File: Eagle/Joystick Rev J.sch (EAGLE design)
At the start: 20 parts, among them U3 LM317-BENT

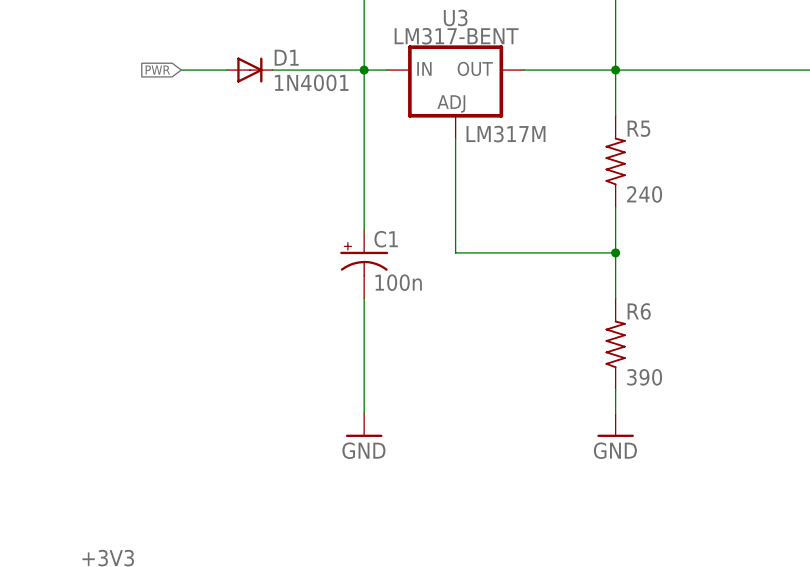
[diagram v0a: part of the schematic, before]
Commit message: changes to BOM for manufacturing
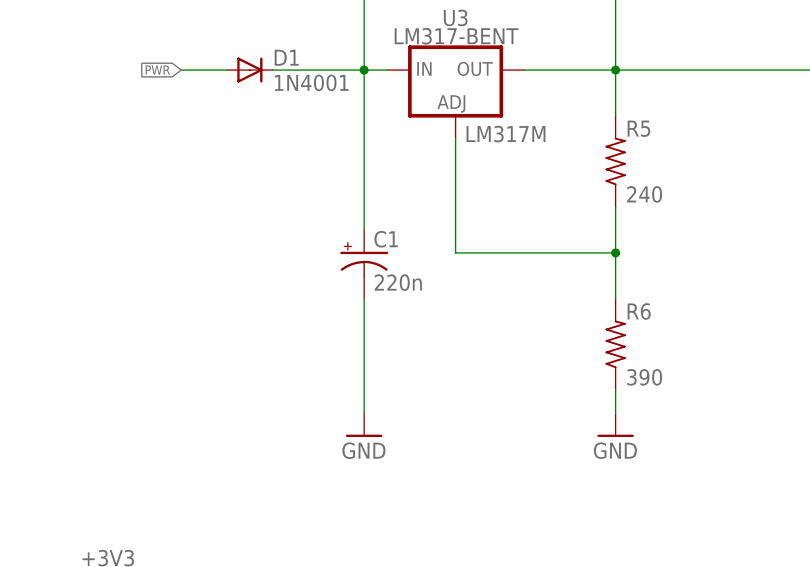
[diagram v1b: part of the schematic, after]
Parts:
- C1: value 100n -> 220n
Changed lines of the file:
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@@
 <grid distance="0.1" unitdist="inch" unit="inch" style="lines" multiple="1" display="no" altdistance="0.01" altunitdist="inch" altunit="inch"/>
 <layers>
-<layer number="1" name="Top" color="4" fill="1" visible="yes" active="no"/>
-<layer number="2" name="Route2" color="16" fill="1" visible="yes" active="no"/>
-<layer number="3" name="Route3" color="4" fill="3" visible="yes" active="no"/>
-<layer number="4" name="Route4" color="1" fill="4" visible="yes" active="no"/>
-<layer number="5" name="Route5" color="4" fill="4" visible="yes" active="no"/>
-<layer number="6" name="Route6" color="1" fill="8" visible="yes" active="no"/>
-<layer number="7" name="Route7" color="4" fill="8" visible="yes" active="no"/>
-<layer number="8" name="Route8" color="1" fill="2" visible="yes" active="no"/>
-<layer number="9" name="Route9" color="4" fill="2" visible="yes" active="no"/>
-<layer number="10" name="Route10" color="1" fill="7" visible="yes" active="no"/>
-<layer number="11" name="Route11" color="4" fill="7" visible="yes" active="no"/>
-<layer number="12" name="Route12" color="1" fill="5" visible="yes" active="no"/>
-<layer number="13" name="Route13" color="4" fill="5" visible="yes" active="no"/>
-<layer number="14" name="Route14" color="1" fill="6" visible="yes" active="no"/>
-<layer number="15" name="Route15" color="23" fill="1" visible="yes" active="no"/>
-<layer number="16" name="Bottom" color="1" fill="1" visible="yes" active="no"/>
-<layer number="17" name="Pads" color="2" fill="1" visible="yes" active="no"/>
-<layer number="18" name="Vias" color="2" fill="1" visible="yes" active="no"/>
-<layer number="19" name="Unrouted" color="6" fill="1" visible="yes" active="no"/>
-<layer number="20" name="Dimension" color="24" fill="1" visible="yes" active="no"/>
-<layer number="21" name="tPlace" color="7" fill="1" visible="yes" active="no"/>
-<layer number="22" name="bPlace" color="7" fill="1" visible="yes" active="no"/>
-<layer number="23" name="tOrigins" color="15" fill="1" visible="yes" active="no"/>
-<layer number="24" name="bOrigins" color="15" fill="1" visible="yes" active="no"/>
-<layer number="25" name="tNames" color="7" fill="1" visible="yes" active="no"/>
-<layer number="26" name="bNames" color="7" fill="1" visible="yes" active="no"/>
-<layer number="27" name="tValues" color="7" fill="1" visible="yes" active="no"/>
-<layer number="28" name="bValues" color="7" fill="1" visible="yes" active="no"/>
+<layer number="1" name="Top" color="4" fill="1" visible="no" active="no"/>
+<layer number="2" name="Route2" color="16" fill="1" visible="no" active="no"/>
+<layer number="3" name="Route3" color="4" fill="3" visible="no" active="no"/>
+<layer number="4" name="Route4" color="1" fill="4" visible="no" active="no"/>
+<layer number="5" name="Route5" color="4" fill="4" visible="no" active="no"/>
+<layer number="6" name="Route6" color="1" fill="8" visible="no" active="no"/>
+<layer number="7" name="Route7" color="4" fill="8" visible="no" active="no"/>
+<layer number="8" name="Route8" color="1" fill="2" visible="no" active="no"/>
+<layer number="9" name="Route9" color="4" fill="2" visible="no" active="no"/>
+<layer number="10" name="Route10" color="1" fill="7" visible="no" active="no"/>
+<layer number="11" name="Route11" color="4" fill="7" visible="no" active="no"/>
+<layer number="12" name="Route12" color="1" fill="5" visible="no" active="no"/>
+<layer number="13" name="Route13" color="4" fill="5" visible="no" active="no"/>
+<layer number="14" name="Route14" color="1" fill="6" visible="no" active="no"/>
+<layer number="15" name="Route15" color="23" fill="1" visible="no" active="no"/>
+<layer number="16" name="Bottom" color="1" fill="1" visible="no" active="no"/>
+<layer number="17" name="Pads" color="2" fill="1" visible="no" active="no"/>
+<layer number="18" name="Vias" color="2" fill="1" visible="no" active="no"/>
+<layer number="19" name="Unrouted" color="6" fill="1" visible="no" active="no"/>
+<layer number="20" name="Dimension" color="24" fill="1" visible="no" active="no"/>
+<layer number="21" name="tPlace" color="7" fill="1" visible="no" active="no"/>
+<layer number="22" name="bPlace" color="7" fill="1" visible="no" active="no"/>
+<layer number="23" name="tOrigins" color="15" fill="1" visible="no" active="no"/>
+<layer number="24" name="bOrigins" color="15" fill="1" visible="no" active="no"/>
+<layer number="25" name="tNames" color="7" fill="1" visible="no" active="no"/>
+<layer number="26" name="bNames" color="7" fill="1" visible="no" active="no"/>
+<layer number="27" name="tValues" color="7" fill="1" visible="no" active="no"/>
+<layer number="28" name="bValues" color="7" fill="1" visible="no" active="no"/>
 <layer number="29" name="tStop" color="7" fill="3" visible="no" active="no"/>
 <layer number="30" name="bStop" color="7" fill="6" visible="no" active="no"/>
@@
 <layer number="35" name="tGlue" color="7" fill="4" visible="no" active="no"/>
 <layer number="36" name="bGlue" color="7" fill="5" visible="no" active="no"/>
-<layer number="37" name="tTest" color="7" fill="1" visible="yes" active="no"/>
-<layer number="38" name="bTest" color="7" fill="1" visible="yes" active="no"/>
+<layer number="37" name="tTest" color="7" fill="1" visible="no" active="no"/>
+<layer number="38" name="bTest" color="7" fill="1" visible="no" active="no"/>
 <layer number="39" name="tKeepout" color="4" fill="11" visible="no" active="no"/>
 <layer number="40" name="bKeepout" color="1" fill="11" visible="no" active="no"/>
@@
 <layer number="44" name="Drills" color="7" fill="1" visible="no" active="no"/>
 <layer number="45" name="Holes" color="7" fill="1" visible="no" active="no"/>
-<layer number="46" name="Milling" color="3" fill="1" visible="yes" active="no"/>
-<layer number="47" name="Measures" color="7" fill="1" visible="yes" active="no"/>
-<layer number="48" name="Document" color="7" fill="1" visible="yes" active="no"/>
-<layer number="49" name="Reference" color="7" fill="1" visible="yes" active="no"/>
-<layer number="50" name="dxf" color="7" fill="1" visible="yes" active="no"/>
-<layer number="51" name="tDocu" color="7" fill="1" visible="yes" active="no"/>
-<layer number="52" name="bDocu" color="7" fill="1" visible="yes" active="no"/>
-<layer number="53" name="tGND_GNDA" color="7" fill="9" visible="yes" active="no"/>
-<layer number="54" name="bGND_GNDA" color="1" fill="9" visible="yes" active="no"/>
-<layer number="56" name="wert" color="7" fill="1" visible="yes" active="no"/>
-<layer number="57" name="tCAD" color="7" fill="1" visible="yes" active="no"/>
-<layer number="58" name="tCAD" color="7" fill="1" visible="yes" active="no"/>
-<layer number="59" name="tCarbon" color="7" fill="1" visible="yes" active="no"/>
-<layer number="60" name="bCarbon" color="7" fill="1" visible="yes" active="no"/>
+<layer number="46" name="Milling" color="3" fill="1" visible="no" active="no"/>
+<layer number="47" name="Measures" color="7" fill="1" visible="no" active="no"/>
+<layer number="48" name="Document" color="7" fill="1" visible="no" active="no"/>
+<layer number="49" name="Reference" color="7" fill="1" visible="no" active="no"/>
+<layer number="50" name="dxf" color="7" fill="1" visible="no" active="no"/>
+<layer number="51" name="tDocu" color="7" fill="1" visible="no" active="no"/>
+<layer number="52" name="bDocu" color="7" fill="1" visible="no" active="no"/>
+<layer number="53" name="tGND_GNDA" color="7" fill="9" visible="no" active="no"/>
+<layer number="54" name="bGND_GNDA" color="1" fill="9" visible="no" active="no"/>
+<layer number="56" name="wert" color="7" fill="1" visible="no" active="no"/>
+<layer number="57" name="tCAD" color="7" fill="1" visible="no" active="no"/>
+<layer number="58" name="tCAD" color="7" fill="1" visible="no" active="no"/>
+<layer number="59" name="tCarbon" color="7" fill="1" visible="no" active="no"/>
+<layer number="60" name="bCarbon" color="7" fill="1" visible="no" active="no"/>
 <layer number="88" name="SimResults" color="9" fill="1" visible="yes" active="yes"/>
 <layer number="89" name="SimProbes" color="9" fill="1" visible="yes" active="yes"/>
@@
 <part name="D1" library="Quantum Projects" library_urn="urn:adsk.eagle:library:19630877" deviceset="1N4000" device="" package3d_urn="urn:adsk.eagle:package:20494835/2" value="1N4001"/>
 <part name="D2" library="Quantum Projects" library_urn="urn:adsk.eagle:library:19630877" deviceset="1N4000" device="" package3d_urn="urn:adsk.eagle:package:20494835/2" value="1N4001"/>
-<part name="C1" library="Quantum Projects" library_urn="urn:adsk.eagle:library:19630877" deviceset="ELECTROLYTIC-CAPACITOR" device="2-4" package3d_urn="urn:adsk.eagle:package:21734552/2" value="100n"/>
+<part name="C1" library="Quantum Projects" library_urn="urn:adsk.eagle:library:19630877" deviceset="ELECTROLYTIC-CAPACITOR" device="2-4" package3d_urn="urn:adsk.eagle:package:21734552/2" value="220n"/>
 <part name="C2" library="Quantum Projects" library_urn="urn:adsk.eagle:library:19630877" deviceset="ELECTROLYTIC-CAPACITOR" device="2-4" package3d_urn="urn:adsk.eagle:package:21734552/2" value="1u"/>
 <part name="M1" library="Quantum Projects" library_urn="urn:adsk.eagle:library:19630877" deviceset="9V-HOLDER" device="M2.5" package3d_urn="urn:adsk.eagle:package:26234240/2"/>
